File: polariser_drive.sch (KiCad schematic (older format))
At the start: 16 parts, among them J1 JACK-C-PC-10A-RA(R), J2 FlatFlex Molex, U1 SPX3819M5-L-5-0, U2 NodeMCU_Amica_R2

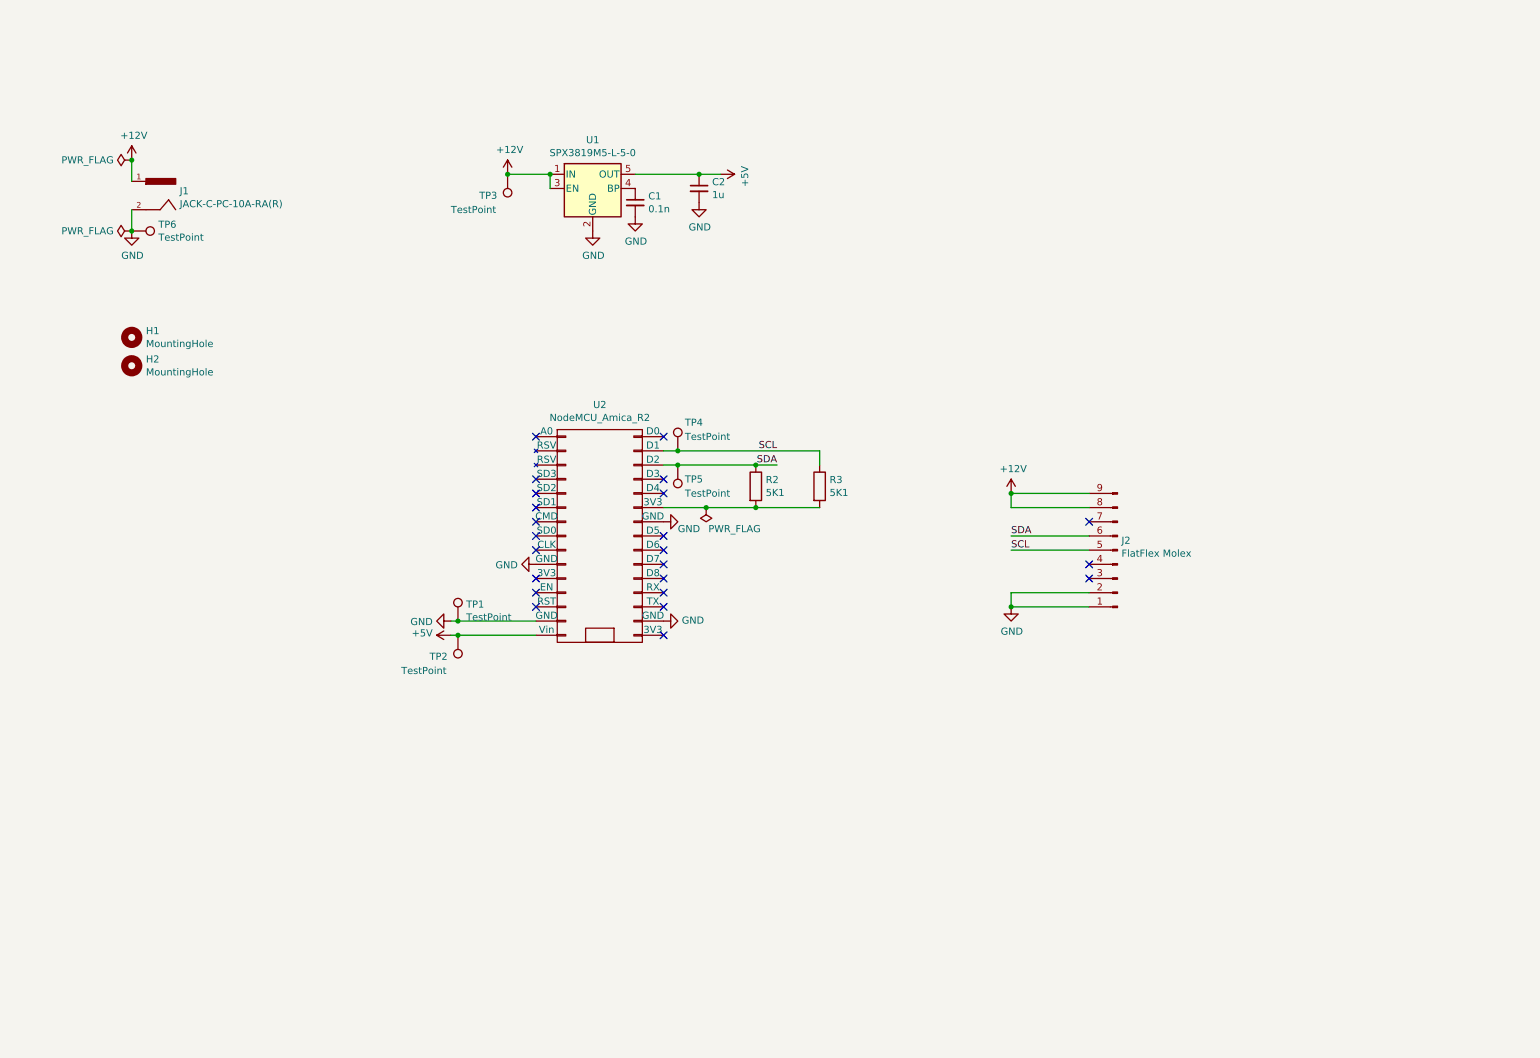
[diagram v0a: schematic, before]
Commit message: add another connector and configurable address lines
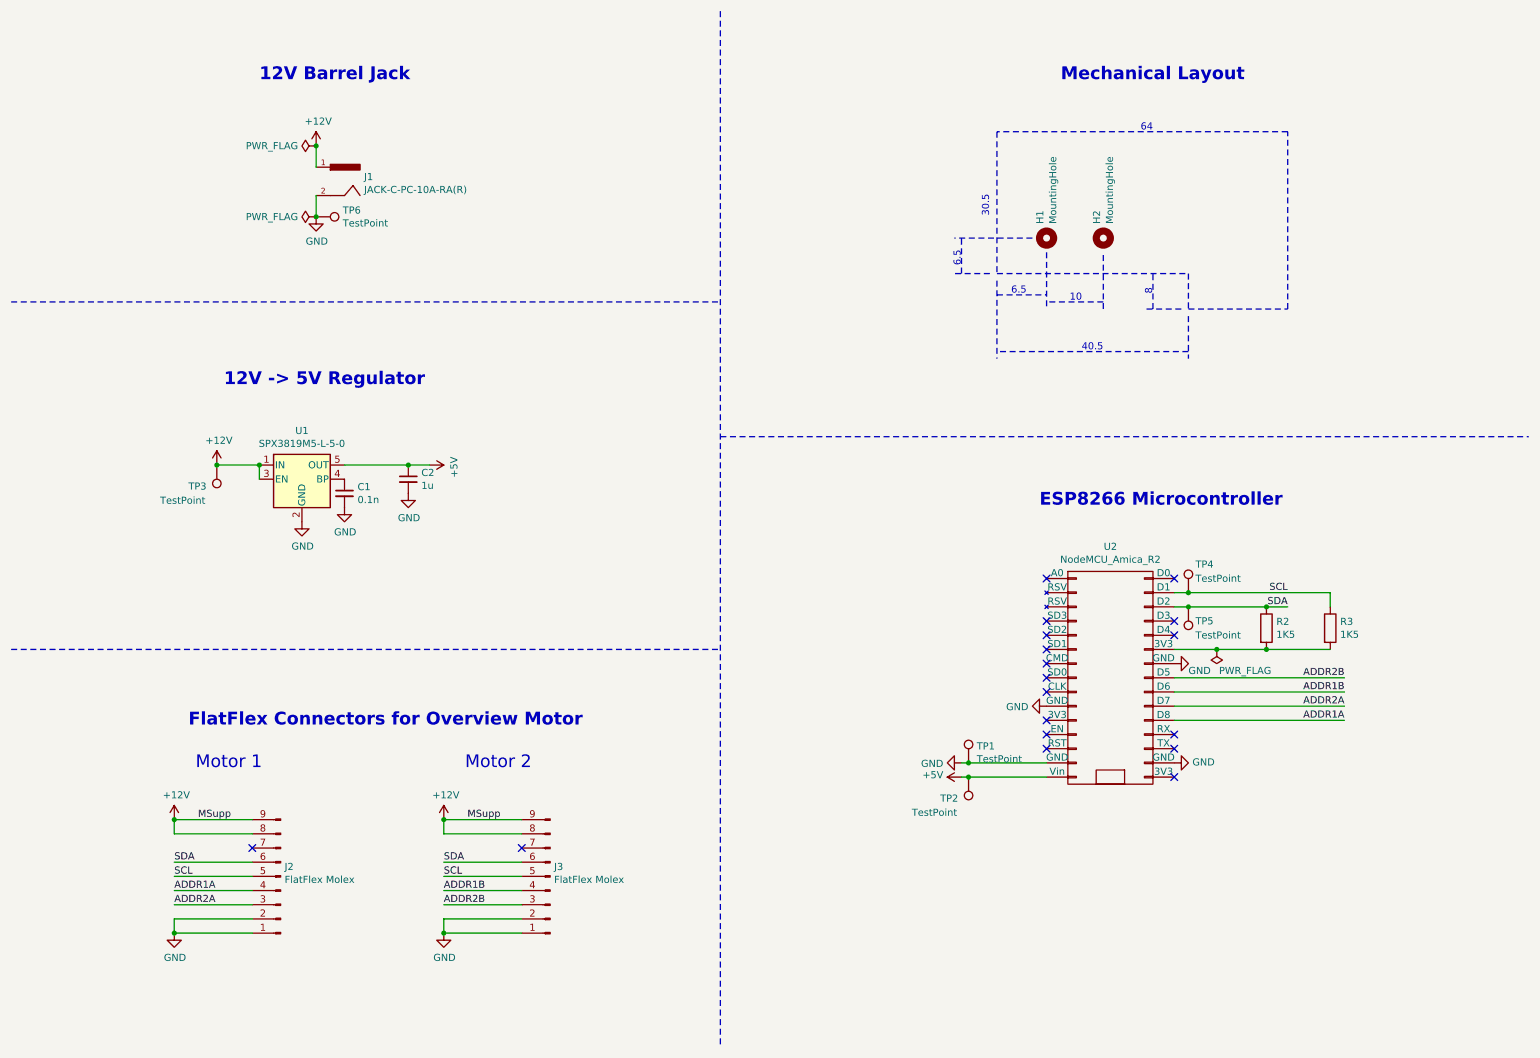
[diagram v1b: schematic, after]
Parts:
- added J3: FlatFlex Molex, Connector_Molex:Molex_Pico-Clasp_202396-0907_1x09-1MP_P1.00mm_Horizontal, symbol Connector:Conn_01x09_Male
- R2, R3: value 5K1 -> 1K5
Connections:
- net +12V: now also J3.8 (Pin_8), J3.9 (Pin_9)
- net GND: now also J3.1 (Pin_1), J3.2 (Pin_2)
- net SCL: now also J3.5 (Pin_5)
- net SDA: now also J3.6 (Pin_6)
- net ADDR1A: now reaches U2.20 (D8)
- net ADDR1A: now also J2.4 (Pin_4)
- net ADDR2A: now reaches U2.21 (D7)
- net ADDR2A: now also J2.3 (Pin_3)
- net ADDR1B: now reaches U2.22 (D6)
- net ADDR1B: now also J3.4 (Pin_4)
- net ADDR2B: now reaches U2.23 (D5)
- net ADDR2B: now also J3.3 (Pin_3)
- no-connect marks 23 -> 18
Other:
- note added: "10"
- note added: "12V -> 5V Regulator"
- note added: "12V Barrel Jack"
- note added: "30.5"
- note added: "40.5\n"
- note added: "6.5"
- note added: "64"
- note added: "8"
- note added: "ESP8266 Microcontroller"
- note added: "FlatFlex Connectors for Overview Motor"
- note added: "Mechanical Layout"
- note added: "Motor 1"
- note added: "Motor 2"
- moved on the sheet: C1, C2, H1, H2, J1, J2, R2, R3, TP1, TP2, TP3, TP4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

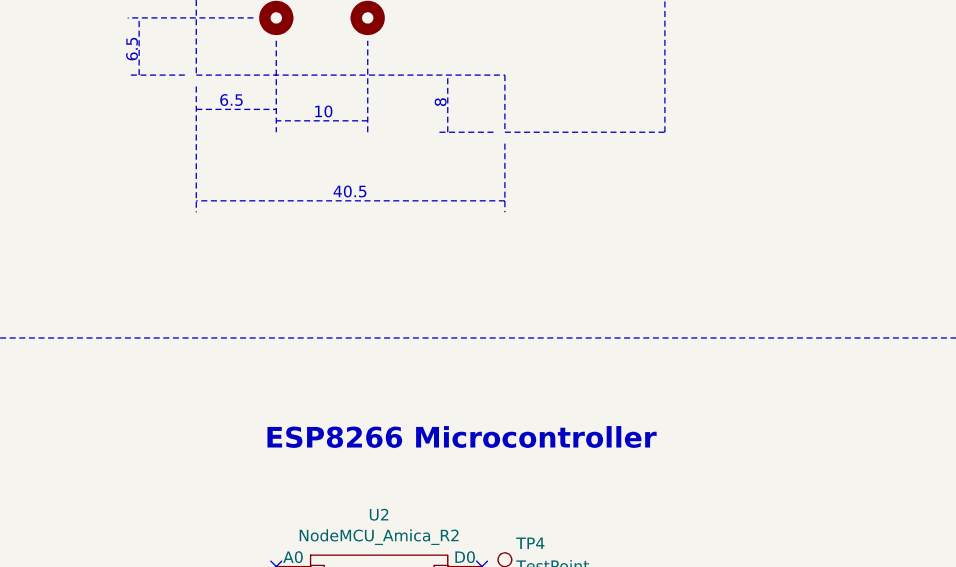
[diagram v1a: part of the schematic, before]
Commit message: add note on sch
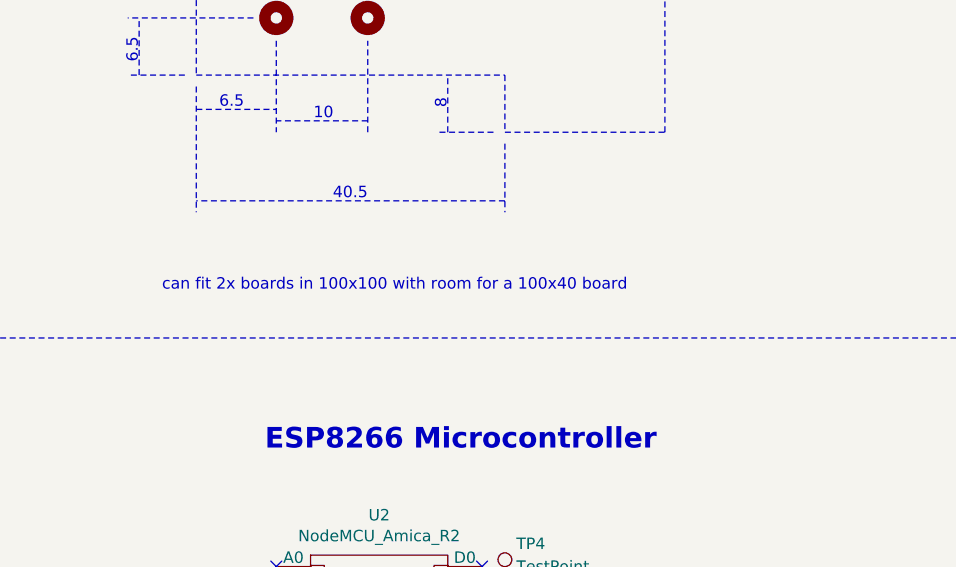
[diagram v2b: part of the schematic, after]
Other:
- note added: "can fit 2x boards in 100x100 with room for a 100x40 board"
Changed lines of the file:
@@
 Wire Notes Line
 	7700 2100 7150 2100
+Text Notes 7300 3300 0    50   ~ 0
+can fit 2x boards in 100x100 with room for a 100x40 board
 $EndSCHEMATC

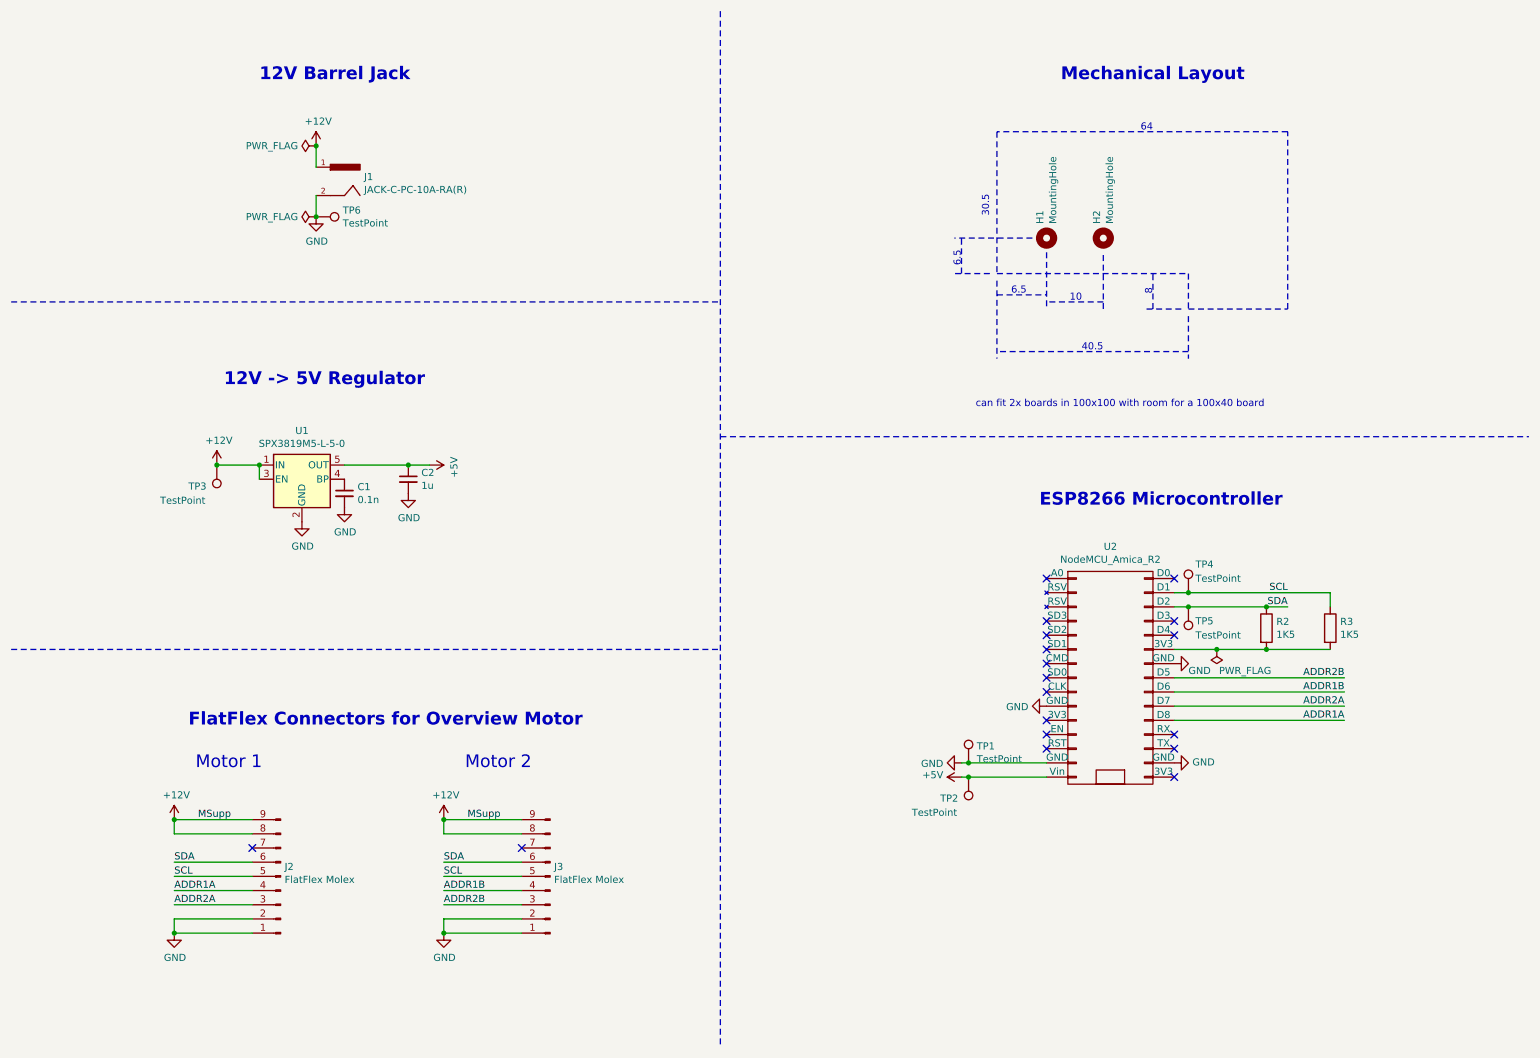
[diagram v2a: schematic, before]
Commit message: stupid rookie footprint error
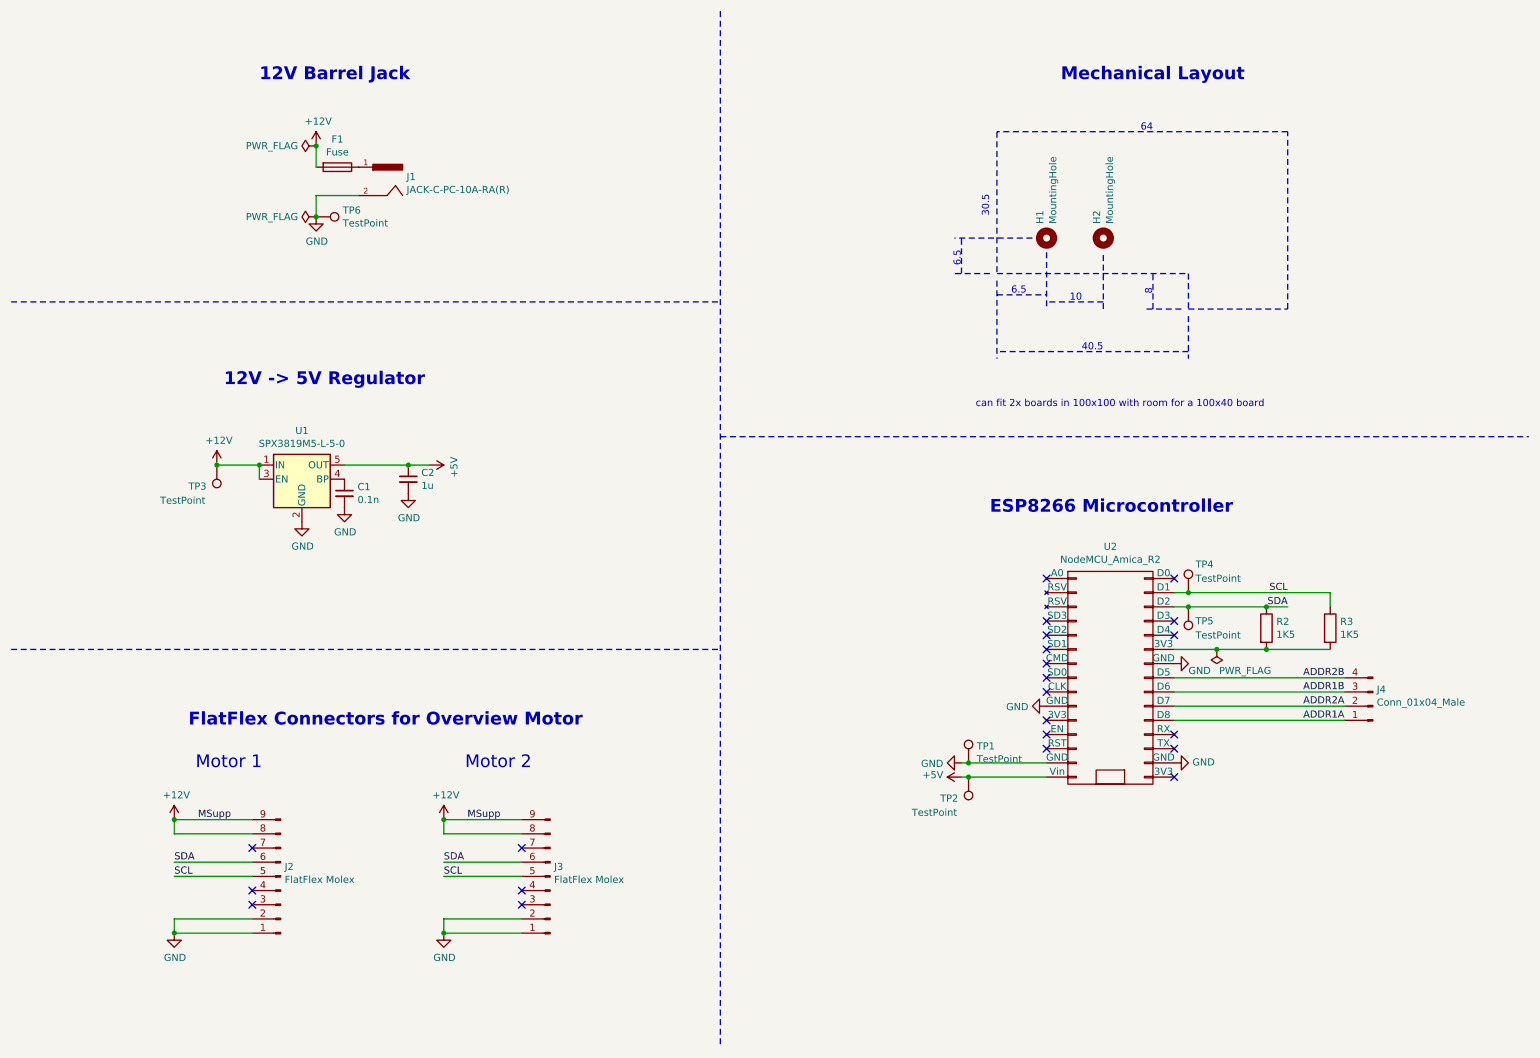
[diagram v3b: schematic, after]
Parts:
- added F1: Fuse, Fuse:Fuse_1206_3216Metric_Pad1.42x1.75mm_HandSolder, symbol Device:Fuse
- added J4: Conn_01x04_Male, Connector_PinHeader_2.54mm:PinHeader_1x04_P2.54mm_Vertical, symbol Connector:Conn_01x04_Male
- C1: footprint Capacitor_SMD:C_0805_2012Metric_Pad1.15x1.40mm_HandSolder -> Fuse:Fuse_1206_3216Metric_Pad1.42x1.75mm_HandSolder
- J2, J3: footprint Connector_Molex:Molex_Pico-Clasp_202396-0907_1x09-1MP_P1.00mm_Horizontal -> flatflex:9pos
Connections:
- net +12V: now also F1.2; no longer J1.1
- net ADDR1A: now also J4.1 (Pin_1); no longer J2.4 (Pin_4)
- net ADDR1B: now also J4.3 (Pin_3); no longer J3.4 (Pin_4)
- net ADDR2A: now also J4.2 (Pin_2); no longer J2.3 (Pin_3)
- net ADDR2B: now also J4.4 (Pin_4); no longer J3.3 (Pin_3)
- new net: F1.1, J1.1
- no-connect marks 18 -> 22
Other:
- moved on the sheet: J1

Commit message: board finished
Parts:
- removed J4: Conn_01x04_Male, Connector_PinHeader_2.54mm:PinHeader_1x04_P2.54mm_Vertical, symbol Connector:Conn_01x04_Male
- removed TP6: TestPoint, TestPoint:TestPoint_Pad_3.0x3.0mm, symbol Connector:TestPoint
- F1: footprint Fuse:Fuse_1206_3216Metric_Pad1.42x1.75mm_HandSolder -> Resistor_THT:R_Axial_DIN0309_L9.0mm_D3.2mm_P12.70mm_Horizontal
- TP4, TP5: footprint TestPoint:TestPoint_Pad_D1.5mm -> Connector_PinHeader_2.54mm:PinHeader_1x01_P2.54mm_Vertical
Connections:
- net +12V: now also J2.1 (Pin_1), J2.2 (Pin_2), J3.1 (Pin_1), J3.2 (Pin_2); no longer J2.8 (Pin_8), J2.9 (Pin_9), J3.8 (Pin_8), J3.9 (Pin_9)
- net GND: now also J2.8 (Pin_8), J2.9 (Pin_9), J3.8 (Pin_8), J3.9 (Pin_9); no longer J2.1 (Pin_1), J2.2 (Pin_2), J3.1 (Pin_1), J3.2 (Pin_2)
- net SDA: now also J2.4 (Pin_4), J3.4 (Pin_4); no longer J2.6 (Pin_6), J3.6 (Pin_6)
- net ADDR1A: no longer names the net of U2.20 (D8)
- net ADDR1B: no longer names the net of U2.22 (D6)
- net ADDR2A: no longer names the net of U2.21 (D7)
- net ADDR2B: no longer names the net of U2.23 (D5)
- no-connect marks 22 -> 26
